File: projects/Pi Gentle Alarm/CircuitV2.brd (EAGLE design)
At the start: 65 x 56 mm, 6 parts, among them IC1 7805T, X1 RASPI_BOARD_B+_E0, X2 22-23-2021

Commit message: Finalization of the Alarm
Only steps are to post process and send
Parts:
- F1: value MINISMDC110F-2 -> (none); device MINISMDC110F-2:FUSC4632X62N -> Test:MF-MSMF260-2
- moved F1 4.00 mm to (25.0, 47.0), turned to 90 degrees
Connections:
- net N$1: now also F1.P$1; no longer F1.1
- net N$2: now also F1.P$2; no longer F1.2
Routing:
- net VCC: track 0.00 -> 29.7 mm
- net N$1: track 0.00 -> 23.4 mm
- net N$2: track 0.00 -> 18.7 mm
- net N$6: track 0.00 -> 8.86 mm
- net GPIO17: track 0.00 -> 7.30 mm
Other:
- board text added: "EMMETT HART RPI GENTLE ALARM HAT 2019"
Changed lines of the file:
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@@
 <wire x1="46" y1="4" x2="45" y2="3" width="0" layer="20" curve="-90"/>
 <wire x1="44" y1="4" x2="45" y2="3" width="0" layer="20" curve="90"/>
+<text x="9" y="10" size="1.778" layer="21">EMMETT HART
+RPI GENTLE ALARM HAT
+2019</text>
 </plain>
 <attributes>
@@
 <attribute name="VALUE" x="42.366" y="29.951" size="1.778" layer="27" ratio="10" rot="R90"/>
 </element>
-<element name="F1" library="MINISMDC110F-2" package="FUSC4632X62N" value="MINISMDC110F-2" x="25" y="43" smashed="yes" rot="R270">
-<attribute name="DESCRIPTION" value="Littelfuse 1.1A Surface Mount Resettable Fuse, 8V dc" x="25" y="43" size="1.778" layer="27" rot="R270" display="off"/>
-<attribute name="HEIGHT" value="0.62mm" x="25" y="43" size="1.778" layer="27" rot="R270" display="off"/>
-<attribute name="MANUFACTURER_NAME" value="LITTELFUSE" x="25" y="43" size="1.778" layer="27" rot="R270" display="off"/>
-<attribute name="MANUFACTURER_PART_NUMBER" value="MINISMDC110F-2" x="25" y="43" size="1.778" layer="27" rot="R270" display="off"/>
-<attribute name="MF" value="RAYCHEM/POLYSWITCH" x="25" y="43" size="1.778" layer="27" rot="R270" display="off"/>
-<attribute name="MOUSER_PART_NUMBER" value="650-MINISMDC110F-2" x="25" y="43" size="1.778" layer="27" rot="R270" display="off"/>
-<attribute name="MOUSER_PRICE-STOCK" value="https://www.mouser.com/Search/Refine.aspx?Keyword=650-MINISMDC110F-2" x="25" y="43" size="1.778" layer="27" rot="R270" display="off"/>
-<attribute name="MPN" value="MINISMDC110F-2" x="25" y="43" size="1.778" layer="27" rot="R270" display="off"/>
-<attribute name="NAME" x="25" y="43" size="1.27" layer="25" rot="R270" align="center"/>
-<attribute name="OC_NEWARK" value="98H4540" x="25" y="43" size="1.778" layer="27" rot="R270" display="off"/>
-<attribute name="VALUE" x="25" y="43" size="1.27" layer="27" rot="R270" align="center"/>
-</element>
+<element name="F1" library="Test" package="MF-MSMF260-2" value="" x="25" y="47" smashed="yes" rot="R90"/>
 </elements>
 <signals>
@@
 <contactref element="LED1" pad="K"/>
 <contactref element="IC1" pad="1"/>
-<wire x1="13.73" y1="35" x2="32.46" y2="30.84" width="0" layer="19" extent="1-1"/>
-<wire x1="10" y1="42.73" x2="13.73" y2="35" width="0" layer="19" extent="1-1"/>
+<wire x1="32.46" y1="30.84" x2="17.89" y2="30.84" width="0.3048" layer="1"/>
+<wire x1="17.89" y1="30.84" x2="13.73" y2="35" width="0.3048" layer="1"/>
+<wire x1="10" y1="42.73" x2="10" y2="38.73" width="0.3048" layer="1"/>
+<wire x1="10" y1="38.73" x2="13.73" y2="35" width="0.3048" layer="1"/>
 </signal>
 <signal name="GPIO17">
 <contactref element="Q1" pad="2"/>
 <contactref element="X1" pad="11"/>
-<wire x1="20.905" y1="44" x2="21.07" y2="51.23" width="0" layer="19" extent="1-1"/>
+<wire x1="20.905" y1="44" x2="20.905" y2="51.065" width="0.3048" layer="16"/>
+<wire x1="20.905" y1="51.065" x2="21.07" y2="51.23" width="0.3048" layer="16"/>
 </signal>
 <signal name="N$6">
 <contactref element="Q1" pad="3"/>
 <contactref element="LED1" pad="A"/>
-<wire x1="16.27" y1="35" x2="19" y2="42.73" width="0" layer="19" extent="1-1"/>
+<wire x1="16.27" y1="35" x2="19" y2="37.73" width="0.3048" layer="1"/>
+<wire x1="19" y1="37.73" x2="19" y2="42.73" width="0.3048" layer="1"/>
 </signal>
 <signal name="N$1">
 <contactref element="X1" pad="2"/>
-<contactref element="F1" pad="1"/>
-<wire x1="8.37" y1="53.77" x2="25" y2="45.065" width="0" layer="19" extent="1-1"/>
+<contactref element="F1" pad="P$1"/>
+<wire x1="7.0746" y1="52.2873375" x2="7.0746" y2="50.1726625" width="0.3048" layer="1"/>
+<wire x1="7.0746" y1="50.1726625" x2="10.2472625" y2="47" width="0.3048" layer="1"/>
+<wire x1="10.2472625" y1="47" x2="25" y2="47" width="0.3048" layer="1"/>
+<wire x1="8.37" y1="53.77" x2="8.37" y2="53.5827375" width="0.3048" layer="1"/>
+<wire x1="8.37" y1="53.5827375" x2="7.0746" y2="52.2873375" width="0.3048" layer="1"/>
 </signal>
 <signal name="N$2">
 <contactref element="IC1" pad="3"/>
-<contactref element="F1" pad="2"/>
-<wire x1="25" y1="40.935" x2="37.54" y2="30.84" width="0" layer="19" extent="1-1"/>
+<contactref element="F1" pad="P$2"/>
+<wire x1="25" y1="44.3" x2="37.54" y2="31.76" width="0.3048" layer="1"/>
+<wire x1="37.54" y1="31.76" x2="37.54" y2="30.84" width="0.3048" layer="1"/>
+</signal>
+<signal name="N$3">
+<via x="15" y="44" extent="1-16" drill="0.508"/>
+</signal>
+<signal name="N$4">
+<via x="23" y="39" extent="1-16" drill="0.508"/>
+</signal>
+<signal name="N$5">
+<via x="8" y="35" extent="1-16" drill="0.508"/>
+</signal>
+<signal name="N$7">
+<via x="24" y="27" extent="1-16" drill="0.508"/>
+</signal>
+<signal name="N$8">
+<via x="29" y="44" extent="1-16" drill="0.508"/>
 </signal>
 </signals>
@@
 </drawing>
 <compatibility>
+<note version="6.3" minversion="6.2.2" severity="warning">
+Since Version 6.2.2 text objects can contain more than one line,
+which will not be processed correctly with this version.
+</note>
 <note version="8.2" severity="warning">
 Since Version 8.2, EAGLE supports online libraries. The ids

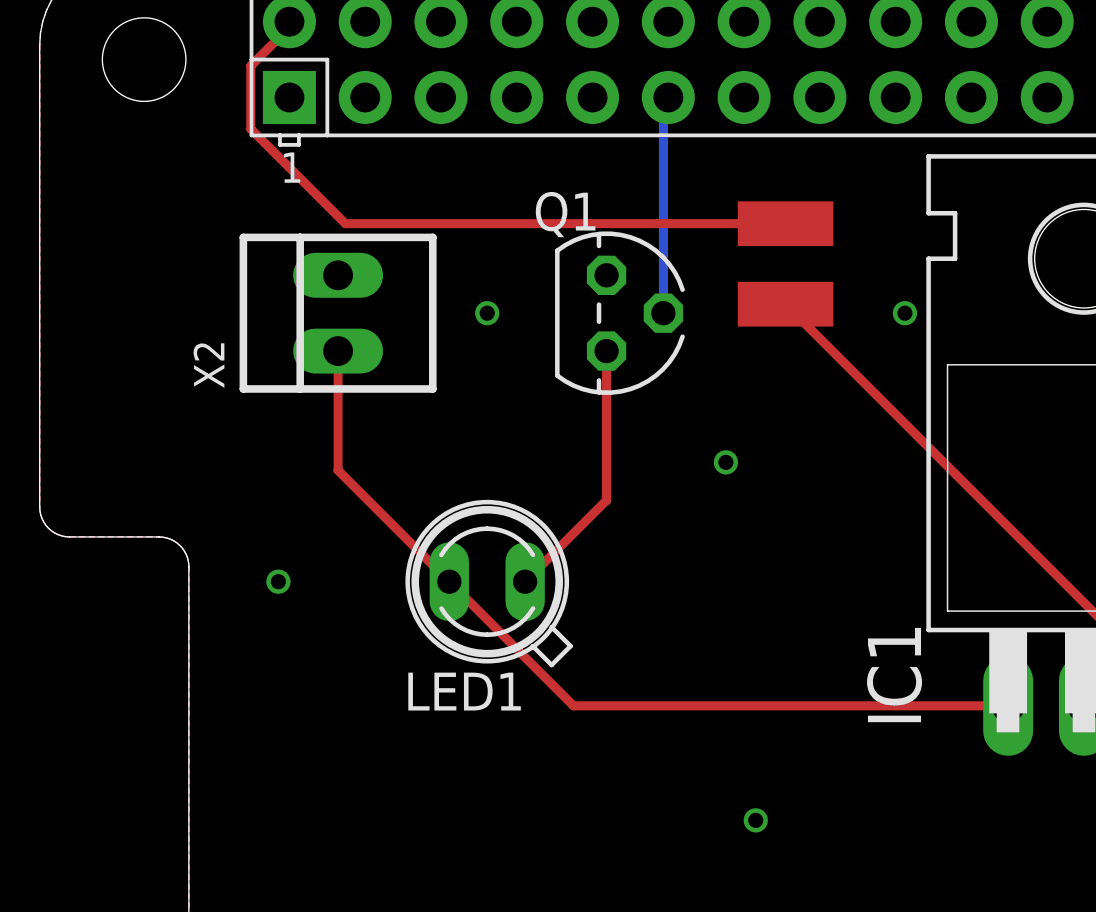
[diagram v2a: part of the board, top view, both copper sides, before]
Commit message: Updated silkscreen
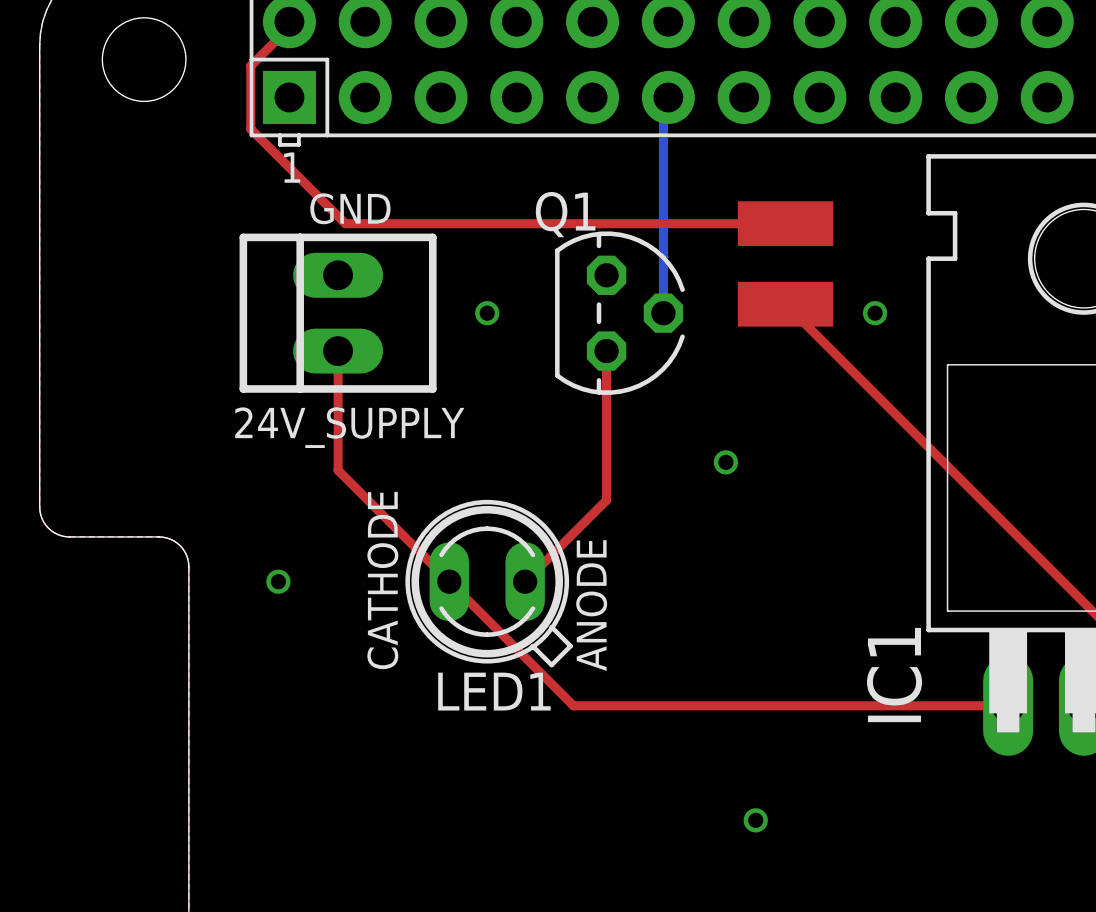
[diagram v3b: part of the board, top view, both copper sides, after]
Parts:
- renumbered X2 to 24V_SUPPLY
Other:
- board text added: "ANODE"
- board text added: "CATHODE"
- board text added: "GND"
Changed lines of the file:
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@@
 RPI GENTLE ALARM HAT
 2019</text>
+<text x="9" y="47" size="1" layer="25">GND</text>
+<text x="19" y="32" size="1" layer="25" rot="R90">ANODE</text>
+<text x="12" y="32" size="1" layer="25" rot="R90">CATHODE</text>
 </plain>
 <attributes>
@@
 <attribute name="OC_NEWARK" value="unknown" x="0" y="0" size="1.778" layer="27" display="off"/>
 </element>
-<element name="X2" library="con-molex" library_urn="urn:adsk.eagle:library:165" package="22-23-2021" package3d_urn="urn:adsk.eagle:package:8078633/1" value="22-23-2021" x="10" y="44" smashed="yes" rot="R90">
+<element name="24V_SUPPLY" library="con-molex" library_urn="urn:adsk.eagle:library:165" package="22-23-2021" package3d_urn="urn:adsk.eagle:package:8078633/1" value="22-23-2021" x="10" y="44" smashed="yes" rot="R90">
 <attribute name="MF" value="MOLEX" x="-2" y="36" size="1.778" layer="27" rot="R90" display="off"/>
 <attribute name="MPN" value="22-23-2021" x="-2" y="36" size="1.778" layer="27" rot="R90" display="off"/>
-<attribute name="NAME" x="6.19" y="41.46" size="1.016" layer="25" ratio="10" rot="R90"/>
+<attribute name="NAME" x="6.46" y="39.81" size="1.016" layer="25" ratio="10"/>
 <attribute name="OC_FARNELL" value="1462926" x="-2" y="36" size="1.778" layer="27" rot="R90" display="off"/>
 <attribute name="OC_NEWARK" value="25C3832" x="-2" y="36" size="1.778" layer="27" rot="R90" display="off"/>
@@
 <attribute name="MF" value="" x="15" y="35" size="1.778" layer="27" rot="R180" display="off"/>
 <attribute name="MPN" value="" x="15" y="35" size="1.778" layer="27" rot="R180" display="off"/>
-<attribute name="NAME" x="16.27" y="31.952" size="1.27" layer="25" ratio="10" rot="R180"/>
+<attribute name="NAME" x="17.27" y="31.952" size="1.27" layer="25" ratio="10" rot="R180"/>
 <attribute name="OC_NEWARK" value="unknown" x="15" y="35" size="1.778" layer="27" rot="R180" display="off"/>
 <attribute name="VALUE" x="16.27" y="39.318" size="1.27" layer="27" ratio="10" rot="R180"/>
@@
 </polygon>
 <contactref element="X1" pad="6"/>
-<contactref element="X2" pad="2"/>
+<contactref element="24V_SUPPLY" pad="2"/>
 <contactref element="Q1" pad="1"/>
 <contactref element="IC1" pad="2"/>
+<via x="24" y="27" extent="1-16" drill="0.508"/>
+<via x="23" y="39" extent="1-16" drill="0.508"/>
+<via x="8" y="35" extent="1-16" drill="0.508"/>
+<via x="15" y="44" extent="1-16" drill="0.508"/>
+<via x="28" y="44" extent="1-16" drill="0.508"/>
 </signal>
 <signal name="3V3">
@@
 </signal>
 <signal name="VCC">
-<contactref element="X2" pad="1"/>
+<contactref element="24V_SUPPLY" pad="1"/>
 <contactref element="LED1" pad="K"/>
 <contactref element="IC1" pad="1"/>
@@
 <wire x1="37.54" y1="31.76" x2="37.54" y2="30.84" width="0.3048" layer="1"/>
 </signal>
-<signal name="N$3">
-<via x="15" y="44" extent="1-16" drill="0.508"/>
-</signal>
-<signal name="N$4">
-<via x="23" y="39" extent="1-16" drill="0.508"/>
-</signal>
-<signal name="N$5">
-<via x="8" y="35" extent="1-16" drill="0.508"/>
-</signal>
-<signal name="N$7">
-<via x="24" y="27" extent="1-16" drill="0.508"/>
-</signal>
-<signal name="N$8">
-<via x="29" y="44" extent="1-16" drill="0.508"/>
-</signal>
 </signals>
